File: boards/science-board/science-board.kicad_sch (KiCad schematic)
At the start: 19 parts, among them J1 Conn_01x02, J10 Conn_01x04, J11 J00-0045NL, J12 Conn_02x03_Counter_Clockwise, J2 Conn_01x08, J3 Conn_01x04, J4 Conn_01x04, J5 Conn_01x08, J6 Conn_01x03, J7 Conn_01x08, J8 Conn_01x08, J9 Conn_01x04, U1 Teensy4.1, U2 LSF0108PWR

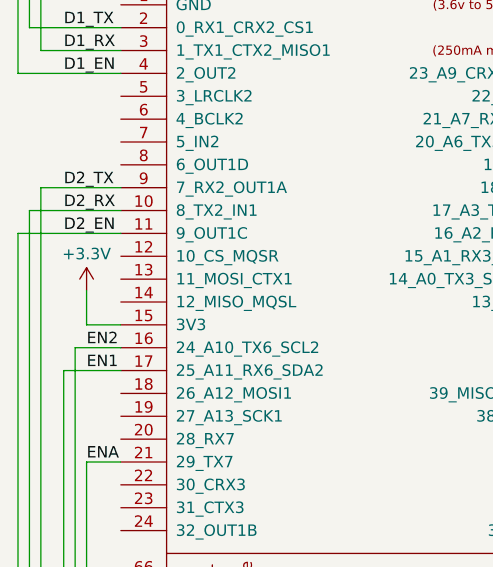
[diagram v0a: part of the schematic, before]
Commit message: updated science board-GND
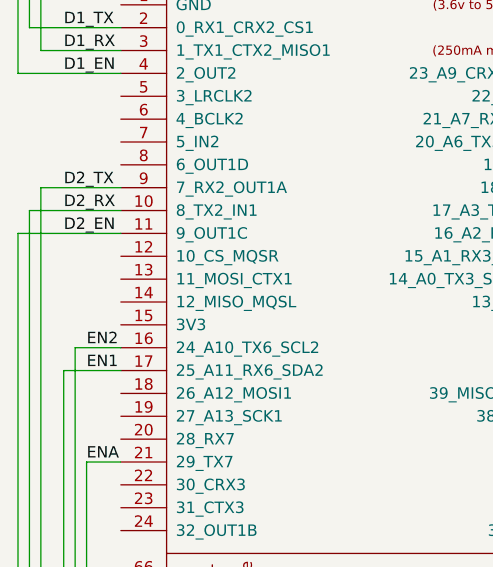
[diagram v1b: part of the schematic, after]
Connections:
- net +3.3V: no longer U1.15 (3V3)
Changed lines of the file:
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@@
 	(wire
 		(pts
-			(xy 38.1 118.11) (xy 38.1 121.92)
-		)
-		(stroke
-			(width 0)
-			(type default)
-		)
-	)
-	(wire
-		(pts
 			(xy 30.48 67.31) (xy 30.48 93.98)
 		)
@@
 	(wire
 		(pts
-			(xy 41.91 121.92) (xy 38.1 121.92)
-		)
-		(stroke
-			(width 0)
-			(type default)
-		)
-	)
-	(wire
-		(pts
 			(xy 176.53 38.1) (xy 176.53 39.37)
 		)
@@
 					(unit 1)
 				)
-			)
-		)
-	)
-	(symbol
-		(lib_id "power:+3.3V")
-		(at 38.1 118.11 0)
-		(unit 1)
-		(exclude_from_sim no)
-		(in_bom yes)
-		(on_board yes)
-		(dnp no)
-		(property "Reference" "#PWR023"
-			(at 38.1 121.92 0)
-			(effects
-				(font
-					(size 1.27 1.27)
-				)
-				(hide yes)
-			)
-		)
-		(property "Value" "+3.3V"
-			(at 38.1 114.046 0)
-			(effects
-				(font
-					(size 1.27 1.27)
-				)
-			)
-		)
-		(property "Footprint" ""
-			(at 38.1 118.11 0)
-			(effects
-				(font
-					(size 1.27 1.27)
-				)
-				(hide yes)
-			)
-		)
-		(property "Datasheet" ""
-			(at 38.1 118.11 0)
-			(effects
-				(font
-					(size 1.27 1.27)
-				)
-				(hide yes)
-			)
-		)
-		(property "Description" "Power symbol creates a global label with name \"+3.3V\""
-			(at 38.1 118.11 0)
-			(effects
-				(font
-					(size 1.27 1.27)
-				)
-				(hide yes)
-			)
-		)
-		(pin "1"
-		)
-		(instances
-			(project "science-board"
-				(path "/a0ddd645-adb6-4647-8179-fc4b155b4dc3"
-					(reference "#PWR023")
-					(unit 1)
-				)

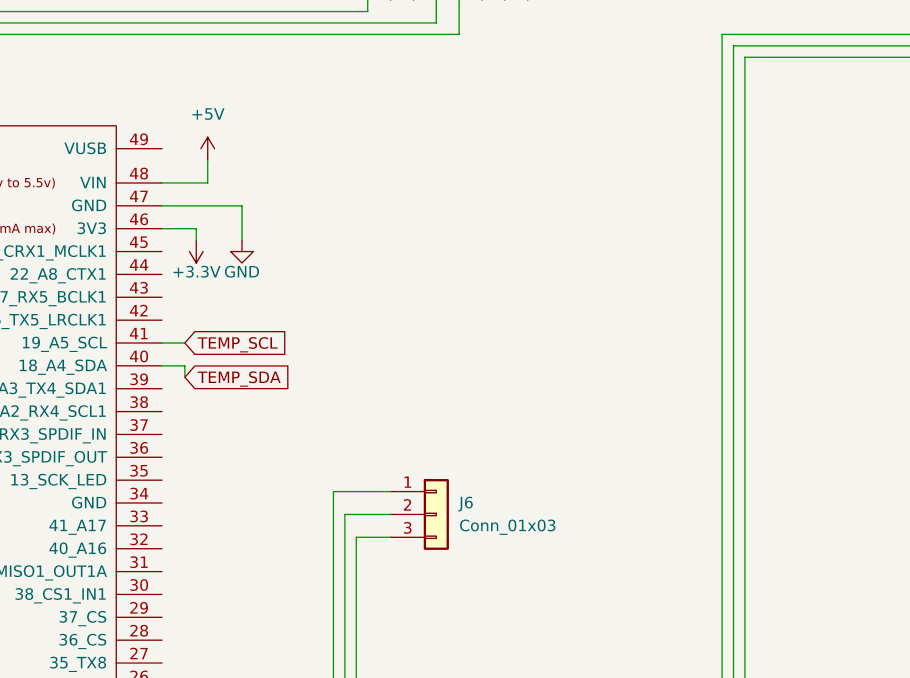
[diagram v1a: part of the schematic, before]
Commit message: Changes to Science and Arm Board
Added pin labels to both boards
Fixed Mislabeled Stepper Board Footprint in Arm board
Added extra digital pins and ground in Science Board
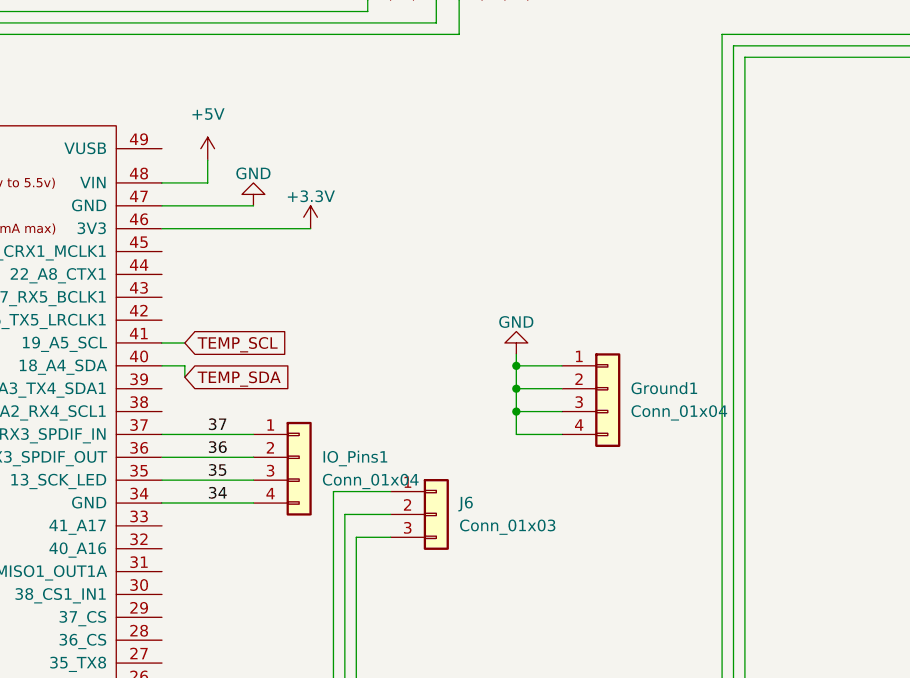
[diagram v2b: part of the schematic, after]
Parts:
- added Ground1, IO_Pins1: Conn_01x04, Connector_JST:JST_EH_B4B-EH-A_1x04_P2.50mm_Vertical, symbol Connector_Generic:Conn_01x04
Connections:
- net GND: now also Ground1.1 (Pin_1), Ground1.2 (Pin_2), Ground1.3 (Pin_3), Ground1.4 (Pin_4)
- net 34: now reaches U1.34 (GND)
- net 34: now also IO_Pins1.4 (Pin_4)
- net 35: now reaches U1.35 (13_SCK_LED)
- net 35: now also IO_Pins1.3 (Pin_3)
- net 36: now reaches U1.36 (14_A0_TX3_SPDIF_OUT)
- net 36: now also IO_Pins1.2 (Pin_2)
- net 37: now reaches U1.37 (15_A1_RX3_SPDIF_IN)
- net 37: now also IO_Pins1.1 (Pin_1)

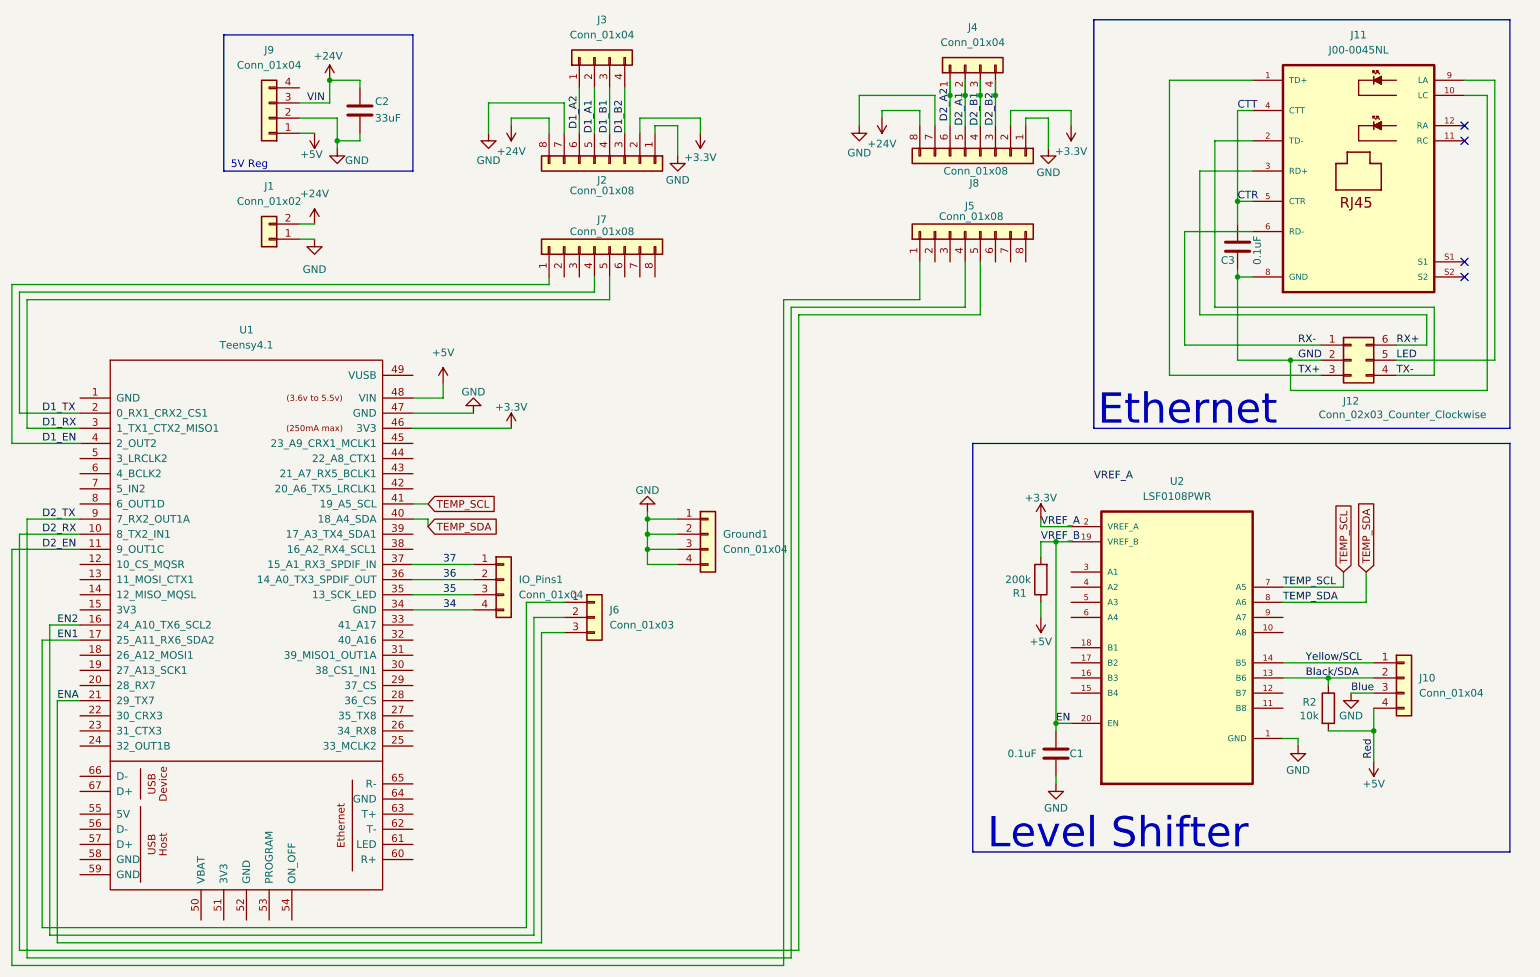
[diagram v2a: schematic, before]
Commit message: Removed I2C level converter from Science Board
BRUH
The temperature probe works running on 3.3V so the level converter for I2C wasn't even necessary on the Science Board. I have removed it from the schematic and updated the PCB layout.
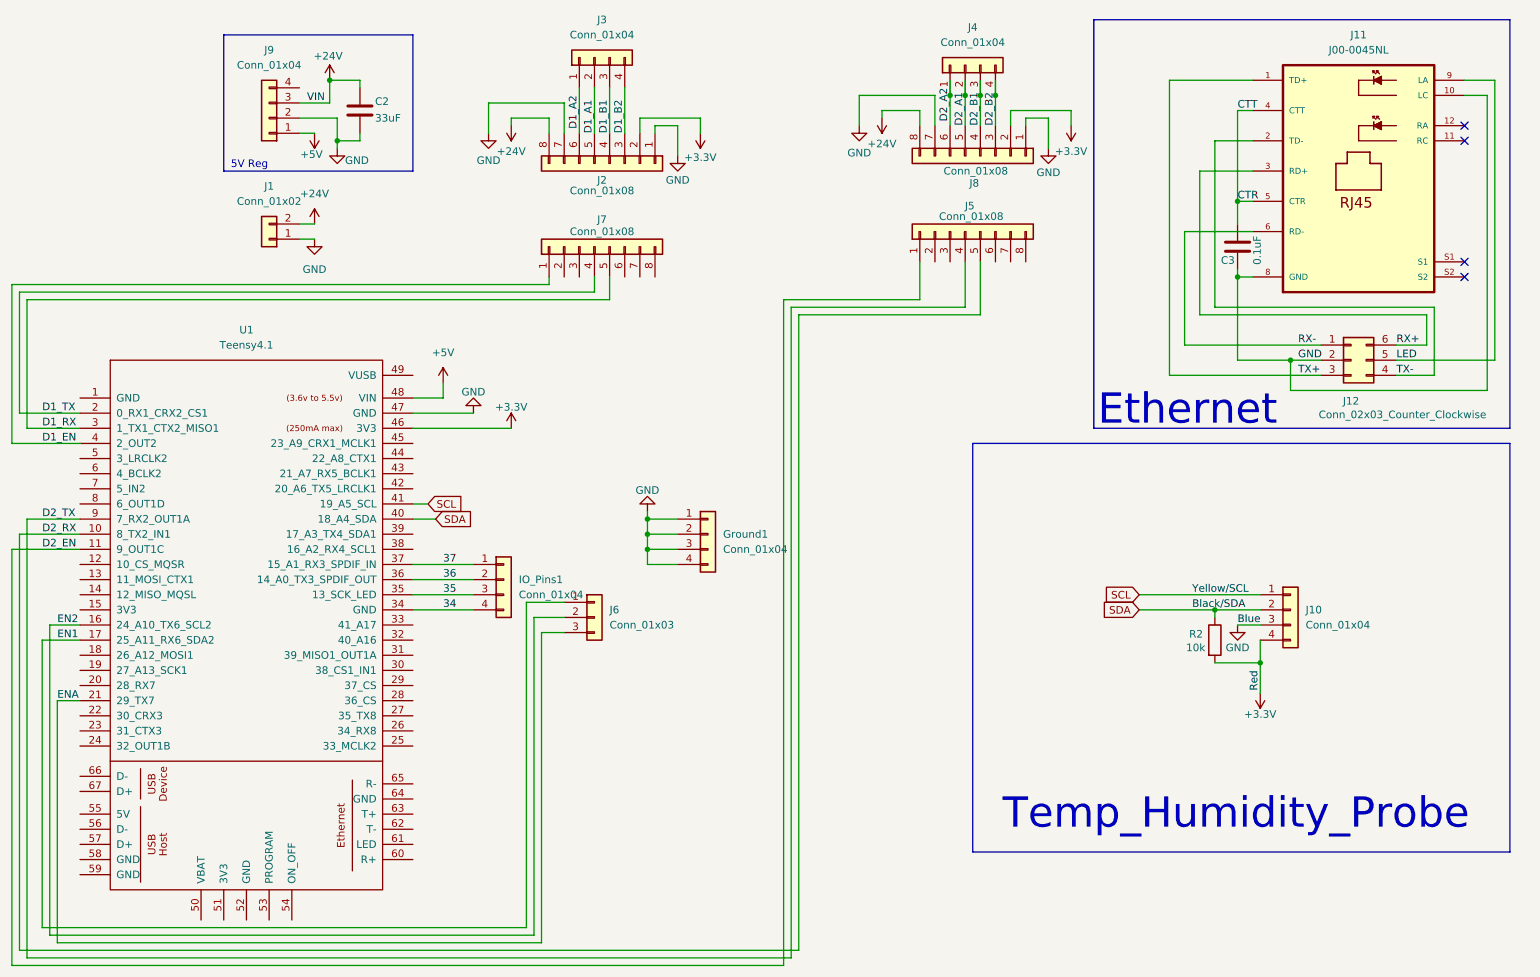
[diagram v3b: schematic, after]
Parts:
- removed C1: 0.1uF, Capacitor_THT:C_Disc_D3.0mm_W1.6mm_P2.50mm, symbol Device:C
- removed R1: 200k, Resistor_THT:R_Axial_DIN0204_L3.6mm_D1.6mm_P5.08mm_Horizontal, symbol Device:R
- removed U2: LSF0108PWR, Package_SO:TSSOP-20_4.4x6.5mm_P0.65mm, symbol LSF0108PWR:LSF0108PWR
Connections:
- net TEMP_SDA is gone; now on net SDA: U1.40 (18_A4_SDA)
- net Yellow/SCL is gone; now on net SCL: J10.1 (Pin_1)
- net +3.3V: now also J10.4 (Pin_4), R2.2
- net +5V: no longer J10.4 (Pin_4), R2.2
- net Black/SDA renamed SDA
- net TEMP_SCL renamed SCL
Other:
- note added: "Temp_Humidity_Probe"
- note removed: "Level Shifter"
- moved on the sheet: J10, R2
